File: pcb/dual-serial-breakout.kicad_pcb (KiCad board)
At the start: 2 copper layers, 36 x 36 mm, 42 parts, among them P1 CONN_01X08, P2 CONN_01X01, P3 CONN_01X01, Q1 BSS138, Q2 BSS138, Q3 BSS138, Q4 BSS138

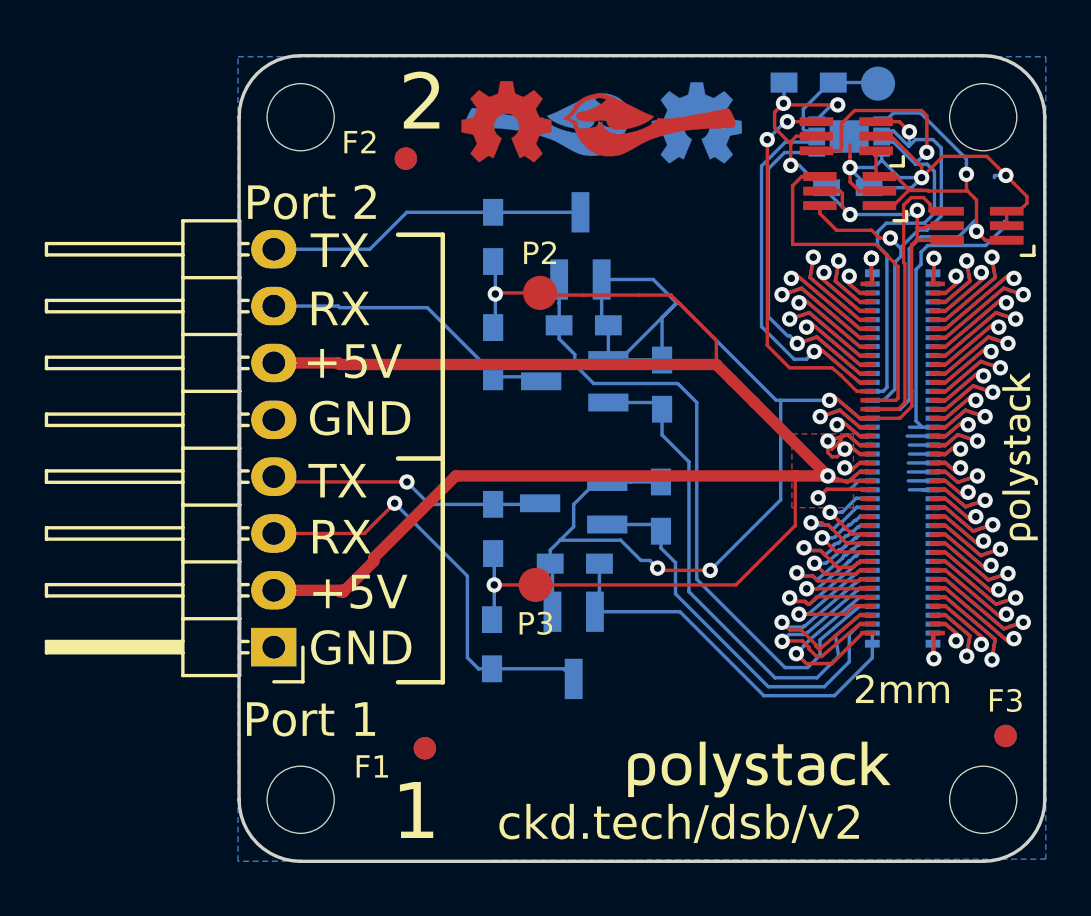
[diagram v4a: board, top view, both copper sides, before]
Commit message: Update polystack logo to bold variant and bump version number.
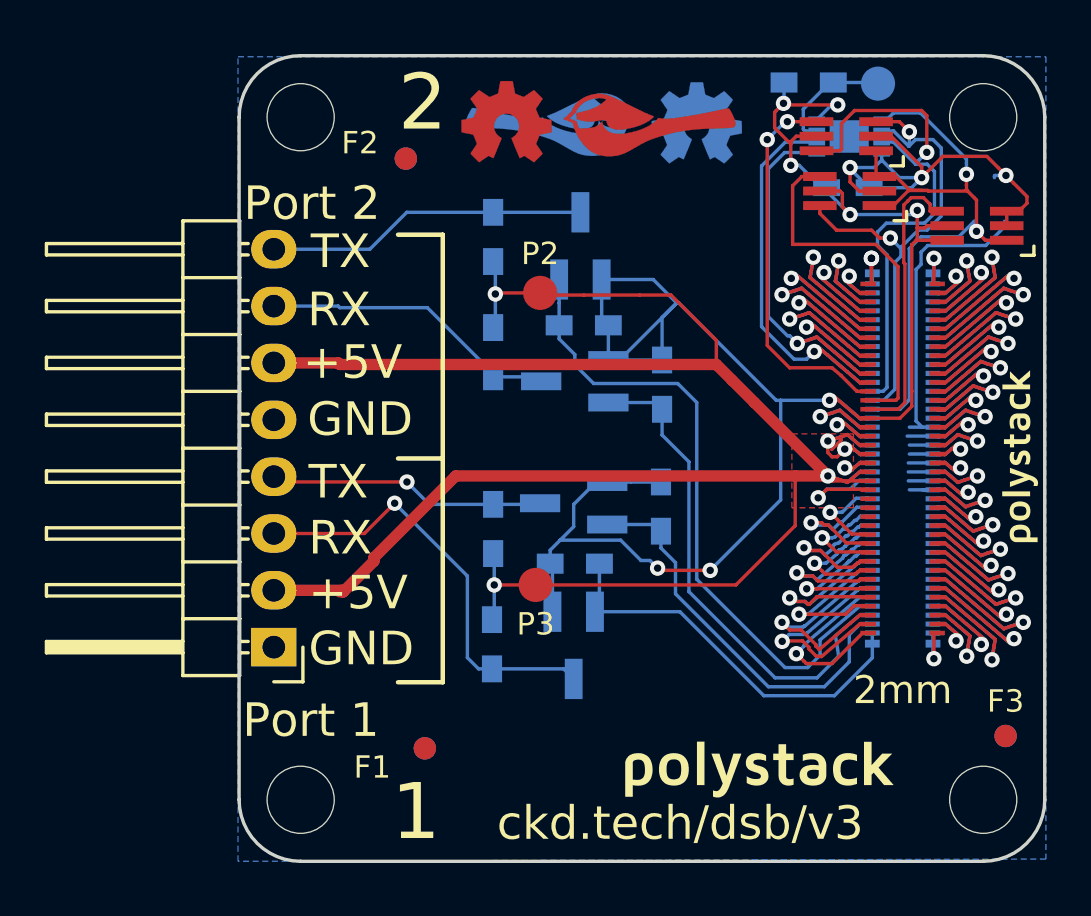
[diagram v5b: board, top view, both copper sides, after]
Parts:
- svg2mod (x2): footprint polystack:polystack-medium-0.625 -> polystack:polystack-bold-0.625
- svg2mod (x2): footprint polystack:polystack-medium-0.4 -> polystack:polystack-bold-0.4
- moved svg2mod 0.10 mm to (164.8, 107.9)
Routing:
- net GNDPWR: track 74.3 -> 73.3 mm
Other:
- board text added: "ckd.tech/dsb/v3"
- board text removed: "ckd.tech/dsb/v2"

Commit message: Add license information to many files. PCB design files are CC-BY and code is MIT license.
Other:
- board text added: "Copyright 2016 Chickadee Tech LLC, <add attributions here> This work is licensed under the Creative Commons Attribution 4.0 International License. To view a copy of this license, visit http://creativecommons.org/licenses/by/4.0/ or send a letter to Creative Commons, PO Box 1866, Mountain View, CA 94042, USA."
- board text added: "Remove all Chickadee Tech LLC trademarks before making your own board. The Chickadee logo and Polystack logo are owned by Chickadee Tech LLC. You may license the Polystack logo for free by emailing support@chickadee.tech and receiving express written permission from Chickadee Tech LLC."
- board text added: "The gear logo is a mark designating open source hardware. Remove it if your design does not comply with the open source hardware definition."
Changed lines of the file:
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@@
     (area 118.127143 74.1 269.404765 178)
     (thickness 1.6)
-    (drawings 62)
+    (drawings 70)
     (tracks 1059)
     (zones 0)
@@
       (xy 2.990233 -0.444493)) (layer B.SilkS) (width 0))
   )
+  (gr_line (start 147.56 78.49) (end 150.77 90.55) (layer Cmts.User) (width 0.2))
+  (gr_line (start 141.28 90.23) (end 147.56 78.49) (layer Cmts.User) (width 0.2))
+  (gr_text "The gear logo is a mark designating open\nsource hardware. Remove it if your design\ndoes not comply with the open source\nhardware definition." (at 137.26 73.34) (layer Cmts.User)
+    (effects (font (size 1.5 1.5) (thickness 0.3)) (justify left))
+  )
+  (gr_line (start 165.95 111.78) (end 167.11 120.93) (layer Cmts.User) (width 0.2))
+  (gr_line (start 166.96 120.93) (end 159.12 121.8) (layer Cmts.User) (width 0.2))
+  (gr_line (start 147.95 95.96) (end 166.96 120.93) (layer Cmts.User) (width 0.2))
+  (gr_text "Remove all Chickadee Tech LLC trademarks\nbefore making your own board. The\nChickadee logo and Polystack logo\nare owned by Chickadee Tech LLC.\n\nYou may license the Polystack logo for\nfree by emailing support@chickadee.tech\nand receiving express written permission\nfrom Chickadee Tech LLC." (at 167.54 124.55) (layer Cmts.User)
+    (effects (font (size 1.5 1.5) (thickness 0.3)) (justify left))
+  )
+  (gr_text "Copyright 2016 Chickadee Tech LLC, <add attributions here>\n\nThis work is licensed under the Creative Commons Attribution 4.0 International License.\nTo view a copy of this license, visit http://creativecommons.org/licenses/by/4.0/\nor send a letter to Creative Commons, PO Box 1866, Mountain View, CA 94042, USA." (at 178.63 173.26) (layer Cmts.User)
+    (effects (font (size 1.5 1.5) (thickness 0.3)) (justify left))
+  )
   (gr_text 2 (at 138.2 92.1) (layer F.SilkS)
     (effects (font (size 2.5 2.5) (thickness 0.4)))
@@
   (gr_line (start 166 92.75) (end 166 123.25) (angle 90) (layer Edge.Cuts) (width 0.15))
   (gr_line (start 132.75 90) (end 163.25 90) (angle 90) (layer Edge.Cuts) (width 0.15))
-  (gr_text dual-serial-breakout (at 187.25 174.25) (layer Cmts.User)
-    (effects (font (size 5 5) (thickness 0.5)) (justify left))
+  (gr_text dual-serial-breakout (at 186.25 189.82) (layer Cmts.User)
+    (effects (font (size 3 3) (thickness 0.5)) (justify left))
   )
   (segment (start 162.95 97.849974) (end 162.95 96.45) (width 0.1524) (layer F.Cu) (net 1))
